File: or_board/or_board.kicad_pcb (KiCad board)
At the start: 2 copper layers, 43.9 x 31.6 mm, 12 parts, among them J1 SJ1-2503A, J2 SJ1-2503A, J3 SJ1-2503A, U1 SN74LS32N

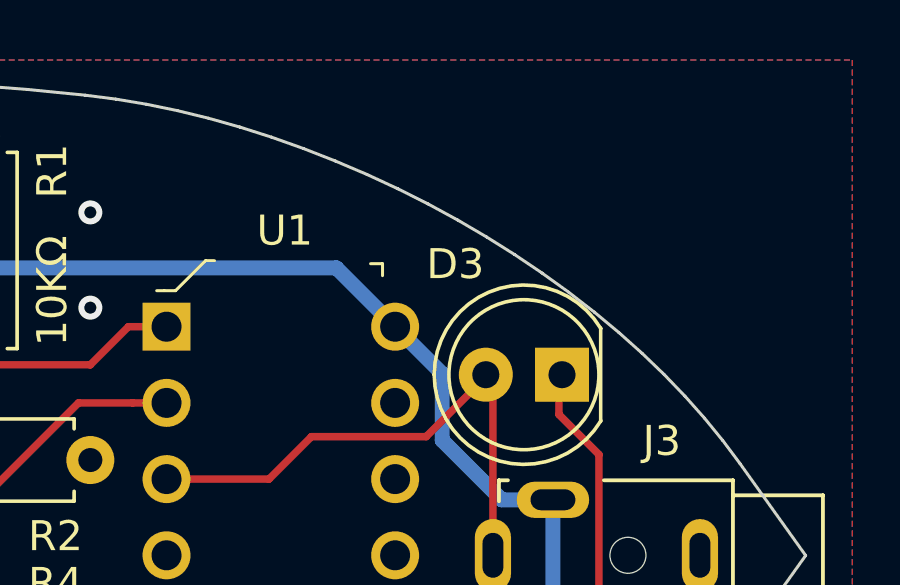
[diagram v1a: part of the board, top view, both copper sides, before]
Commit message: Added truth table silk to and/or boards
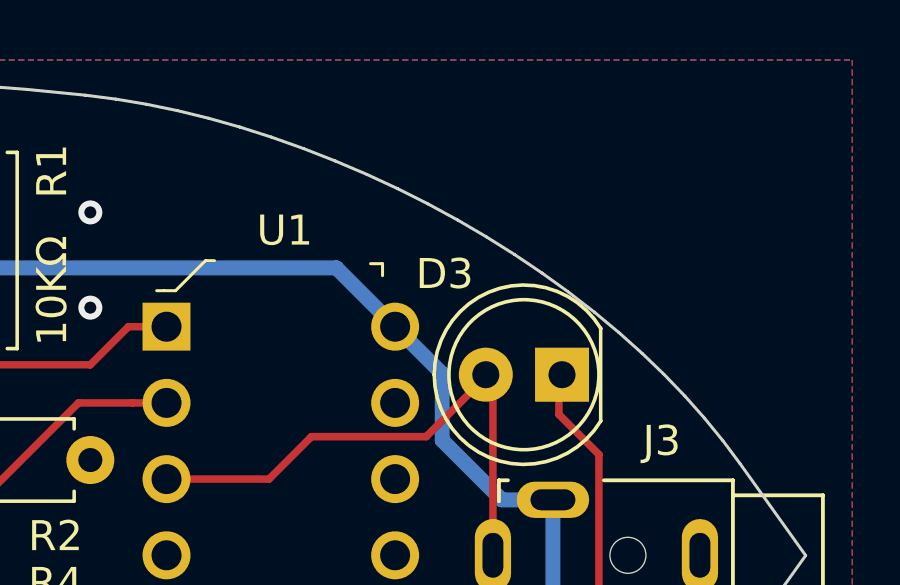
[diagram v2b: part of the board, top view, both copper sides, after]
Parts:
- added Ref**: Val**, conduWIT_parts:or_truth_table, B.Cu at (140.5, 74.8)

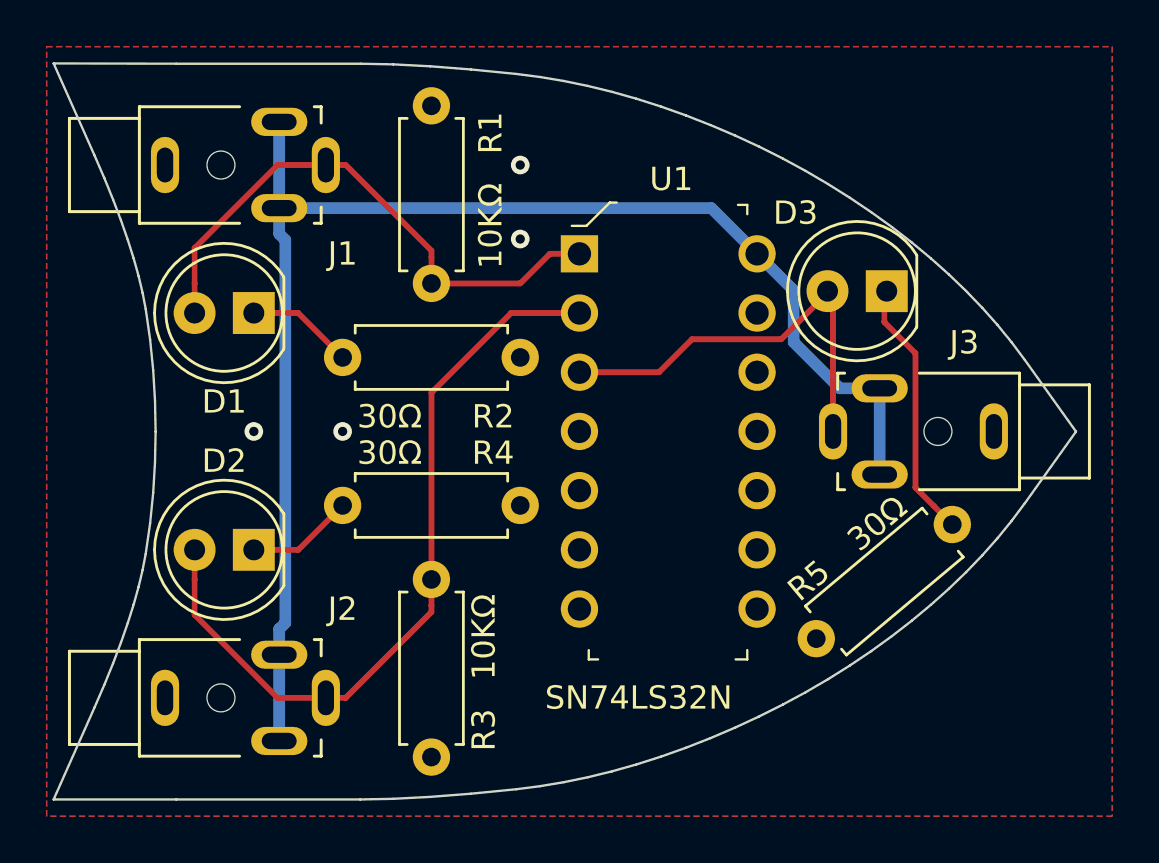
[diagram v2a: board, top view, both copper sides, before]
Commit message: Increased track width and clearance
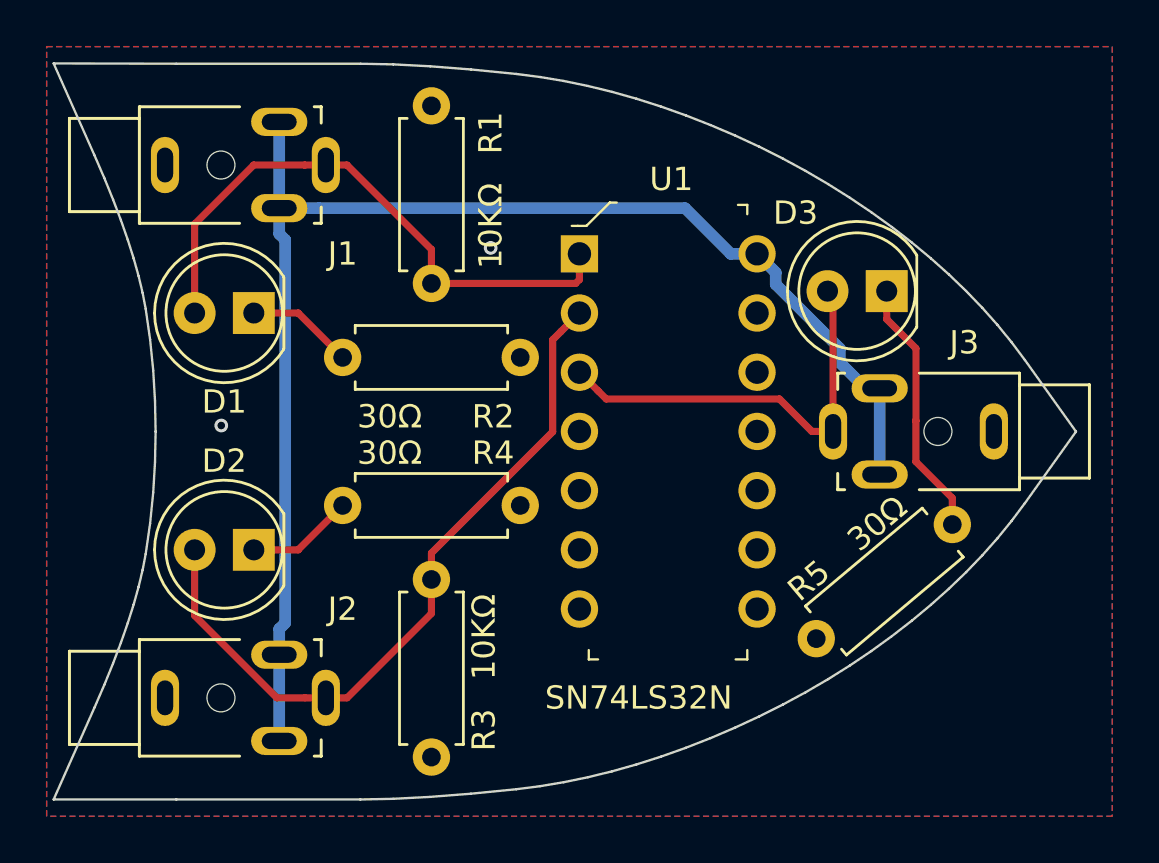
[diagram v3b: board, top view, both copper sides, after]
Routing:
- net Net-(D2-Pad2): track 33.1 -> 31.5 mm
- net Net-(D1-Pad2): track 24.2 -> 25.5 mm
- net +5V: track 60.7 -> 60.1 mm
- net GND: vias 4 -> 2
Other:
- net class Default: clearance 0.2 -> 0.19558; trace_width 0.25 -> 0.3048; via_dia 0.8 -> 0.5842; via_drill 0.4 -> 0.3302
- rule pad_to_mask_clearance: 0.051 -> 0
- rule trace_clearance: 0.2 -> 0.19558
- rule trace_min: 0.2 -> 0.3048
- rule via_min_drill: 0.3 -> 0.3302
- rule via_min_size: 0.4 -> 0.5842

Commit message: Final silkscreen touch-up
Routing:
- net GND: vias 2 -> 3
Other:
- board text added: "or_board 1.0.0 03/2020"
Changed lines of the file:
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@@
   (general
     (thickness 1.6)
-    (drawings 89)
-    (tracks 62)
+    (drawings 90)
+    (tracks 63)
     (zones 0)
     (modules 13)
@@
     (visible_elements 7FFFFFFF)
     (pcbplotparams
-      (layerselection 0x010fc_ffffffff)
-      (usegerberextensions false)
+      (layerselection 0x010f0_ffffffff)
+      (usegerberextensions true)
       (usegerberattributes false)
       (usegerberadvancedattributes false)
@@
       (outputformat 1)
       (mirror false)
-      (drillshape 1)
+      (drillshape 0)
       (scaleselection 1)
-      (outputdirectory ""))
+      (outputdirectory "mfg/"))
   )
   (net 0 "")
@@
     )
   )
+  (gr_text "or_board\n1.0.0\n03/2020" (at 126.873 74.93 90) (layer B.SilkS)
+    (effects (font (size 1 1) (thickness 0.15)) (justify mirror))
+  )
   (gr_line (start 119.681048 59.1412) (end 121.436344 63.089861) (layer Edge.Cuts) (width 0.1))
   (gr_line (start 121.436344 63.089861) (end 121.8546 64.056394) (layer Edge.Cuts) (width 0.1))
@@
   (segment (start 156.67599 74.470997) (end 156.672019 74.474968) (width 0.3048) (layer F.Cu) (net 6))
   (segment (start 155.4226 68.9102) (end 155.4226 70.115) (width 0.3048) (layer F.Cu) (net 6))
-  (via (at 126.873 74.676) (size 0.5842) (drill 0.3302) (layers F.Cu B.Cu) (net 7))
+  (via (at 126.873 72.136) (size 0.5842) (drill 0.3302) (layers F.Cu B.Cu) (net 7))
   (via (at 138.43 67.056) (size 0.5842) (drill 0.3302) (layers F.Cu B.Cu) (net 7))
+  (via (at 145.923 70.231) (size 0.5842) (drill 0.3302) (layers F.Cu B.Cu) (net 7))
   (segment (start 155.12 76.78) (end 155.12 73.08) (width 0.5) (layer B.Cu) (net 8))
   (segment (start 150.659999 68.109999) (end 149.86 67.31) (width 0.5) (layer B.Cu) (net 8))

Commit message: Updated OR board resistor values
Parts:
- R1, R3: value 10KΩ -> 5.1KΩ
- R2, R4, R5: value 30Ω -> 150Ω
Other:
- net class Default removed

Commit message: Fix version
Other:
- board text added: "or_board 1.0.1 01/2023"
- board text removed: "or_board 1.0.0 03/2020"
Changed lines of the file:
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@@
   (gr_line (start 143.640116 60.361059) (end 142.601845 60.107363) (layer "Edge.Cuts") (width 0.1))
   (gr_line (start 153.84392 84.971113) (end 154.756947 84.355576) (layer "Edge.Cuts") (width 0.1))
-  (gr_text "or_board\n1.0.0\n03/2020" (at 126.873 74.93 90) (layer "B.SilkS")
+  (gr_text "or_board\n1.0.1\n01/2023" (at 126.873 74.93 90) (layer "B.SilkS")
     (effects (font (size 1 1) (thickness 0.15)) (justify mirror))
   )
